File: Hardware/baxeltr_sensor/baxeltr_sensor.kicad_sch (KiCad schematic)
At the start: 0 parts

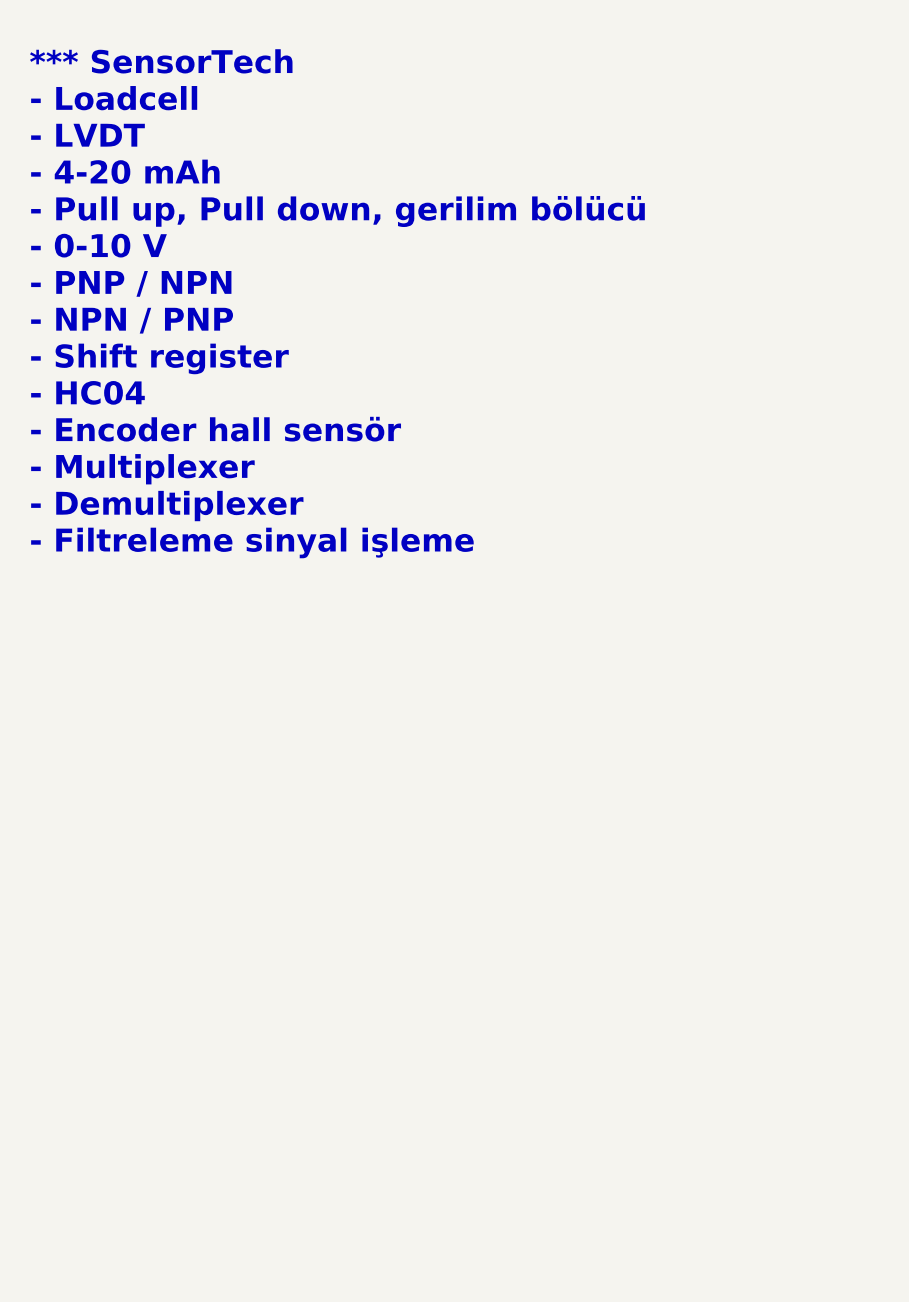
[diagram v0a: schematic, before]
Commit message: şematik güncellendi
4-20mah ve temperature şematikleri eklendi, ltsipce simülasyonları eklendi
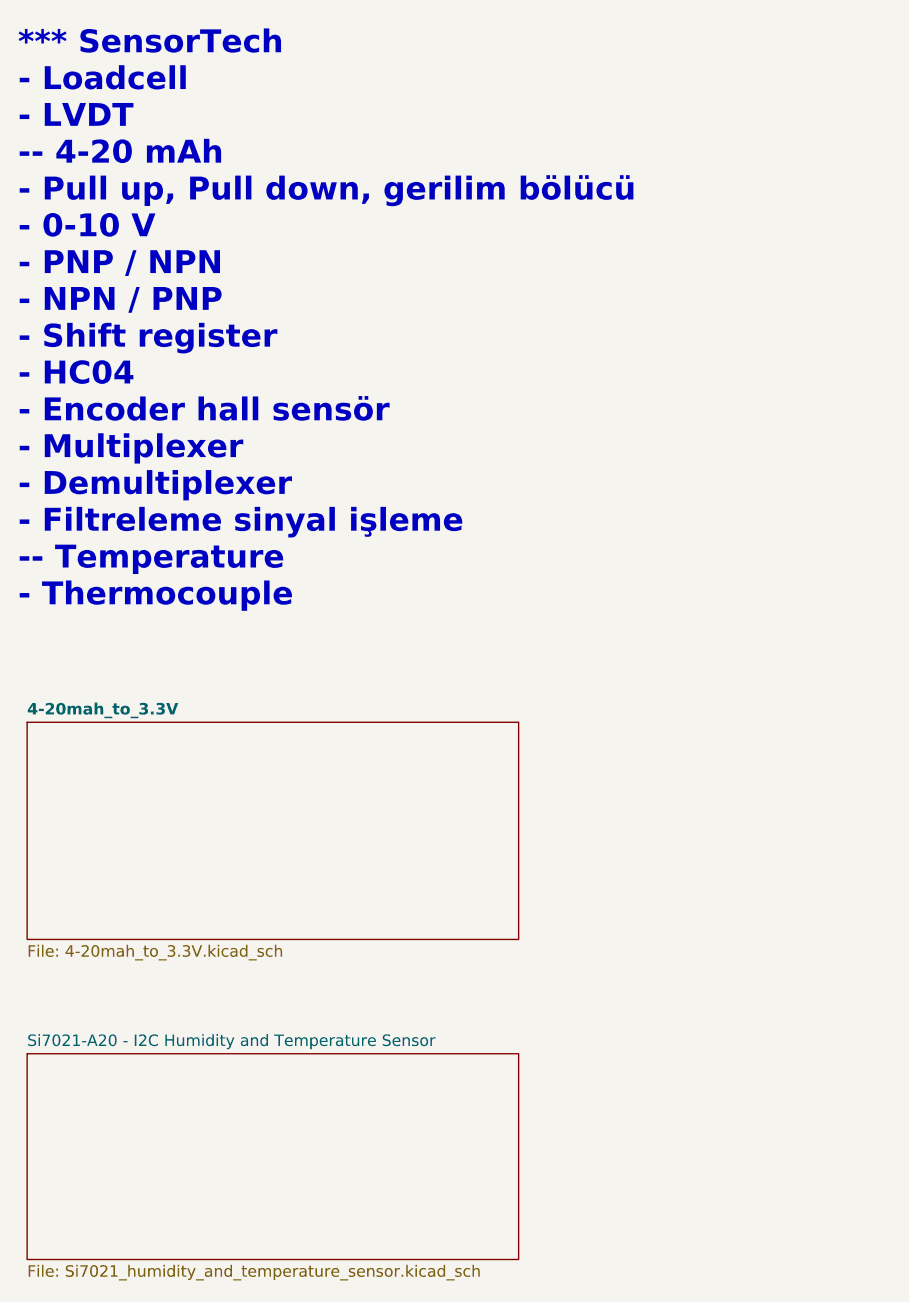
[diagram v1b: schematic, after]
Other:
- added sheet 4-20mah_to_3.3V (4-20mah_to_3.3V.kicad_sch)
- added sheet Si7021-A20 - I2C Humidity and Temperature Sensor (Si7021_humidity_and_temperature_sensor.kicad_sch)
- note added: "*** SensorTech - Loadcell - LVDT -- 4-20 mAh - Pull up, Pull down, gerilim bölücü - 0-10 V - PNP / NPN - NPN / PNP - Shift register - HC04 - Encoder hall sensör - Multiplexer - Demultiplexer - Filtreleme sinyal işleme -- Temperature - Thermocouple"
- note removed: "*** SensorTech - Loadcell - LVDT - 4-20 mAh - Pull up, Pull down, gerilim bölücü - 0-10 V - PNP / NPN - NPN / PNP - Shift register - HC04 - Encoder hall sensör - Multiplexer - Demultiplexer - Filtreleme sinyal işleme"
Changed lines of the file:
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@@
 	(generator_version "9.0")
 	(paper "A3")
-	(text "*** SensorTech\n- Loadcell \n- LVDT\n- 4-20 mAh\n- Pull up, Pull down, gerilim bölücü\n- 0-10 V\n- PNP / NPN\n- NPN / PNP\n- Shift register\n- HC04\n- Encoder hall sensör\n- Multiplexer\n- Demultiplexer\n- Filtreleme sinyal işleme\n"
+	(text "*** SensorTech\n- Loadcell \n- LVDT\n-- 4-20 mAh\n- Pull up, Pull down, gerilim bölücü\n- 0-10 V\n- PNP / NPN\n- NPN / PNP\n- Shift register\n- HC04\n- Encoder hall sensör\n- Multiplexer\n- Demultiplexer\n- Filtreleme sinyal işleme\n-- Temperature\n- Thermocouple\n"
 		(exclude_from_sim no)
-		(at 24.384 46.228 0)
+		(at 23.114 48.006 0)
 		(effects
 			(font
@@
 		)
 	)
+	(sheet
+		(at 24.13 129.54)
+		(size 54.61 22.86)
+		(exclude_from_sim no)
+		(in_bom yes)
+		(on_board yes)
+		(dnp no)
+		(fields_autoplaced yes)
+		(stroke
+			(width 0.1524)
+			(type solid)
+		)
+		(fill
+			(color 0 0 0 0.0000)
+		)
+		(property "Sheetname" "Si7021-A20 - I2C Humidity and Temperature Sensor"
+			(at 24.13 128.8284 0)
+			(effects
+				(font
+					(size 1.27 1.27)
+				)
+				(justify left bottom)
+			)
+		)
+		(property "Sheetfile" "Si7021_humidity_and_temperature_sensor.kicad_sch"
+			(at 24.13 152.9846 0)
+			(effects
+				(font
+					(size 1.27 1.27)
+				)
+				(justify left top)
+			)
+		)
+		(property "Field2" ""
+			(at 24.13 129.54 0)
+			(effects
+				(font
+					(size 1.27 1.27)
+				)
+			)
+		)
+		(instances
+			(project "baxeltr_sensor"
+				(path "/c48f3267-cc9a-42ff-99ff-5758205a3e4c"
+					(page "3")
+				)
+			)
+		)
+	)
+	(sheet
+		(at 24.13 92.71)
+		(size 54.61 24.13)
+		(exclude_from_sim no)
+		(in_bom yes)
+		(on_board yes)
+		(dnp no)
+		(fields_autoplaced yes)
+		(stroke
+			(width 0.1524)
+			(type solid)
+		)
+		(fill
+			(color 0 0 0 0.0000)
+		)
+		(property "Sheetname" "4-20mah_to_3.3V"
+			(at 24.13 91.9984 0)
+			(effects
+				(font
+					(size 1.27 1.27)
+					(thickness 0.254)
+					(bold yes)
+				)
+				(justify left bottom)
+			)
+		)
+		(property "Sheetfile" "4-20mah_to_3.3V.kicad_sch"
+			(at 24.13 117.4246 0)
+			(effects
+				(font
+					(size 1.27 1.27)
+				)
+				(justify left top)
+			)
+		)
+		(instances
+			(project "baxeltr_sensor"
+				(path "/c48f3267-cc9a-42ff-99ff-5758205a3e4c"
+					(page "2")
+				)
+			)
+		)
+	)
